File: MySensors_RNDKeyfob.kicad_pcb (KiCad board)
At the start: 2 copper layers, 27 x 42.9 mm, 21 parts, among them P1 CONN_01X01, P2 CONN_02X03, SW1 SW_SPST, SW2 SW_SPST, SW3 SW_SPST, SW4 SW_SPST, SW5 SW_SPST, U1 ATSHA204A, U2 RFM69HCW, U3 ATMEGA328P-MU

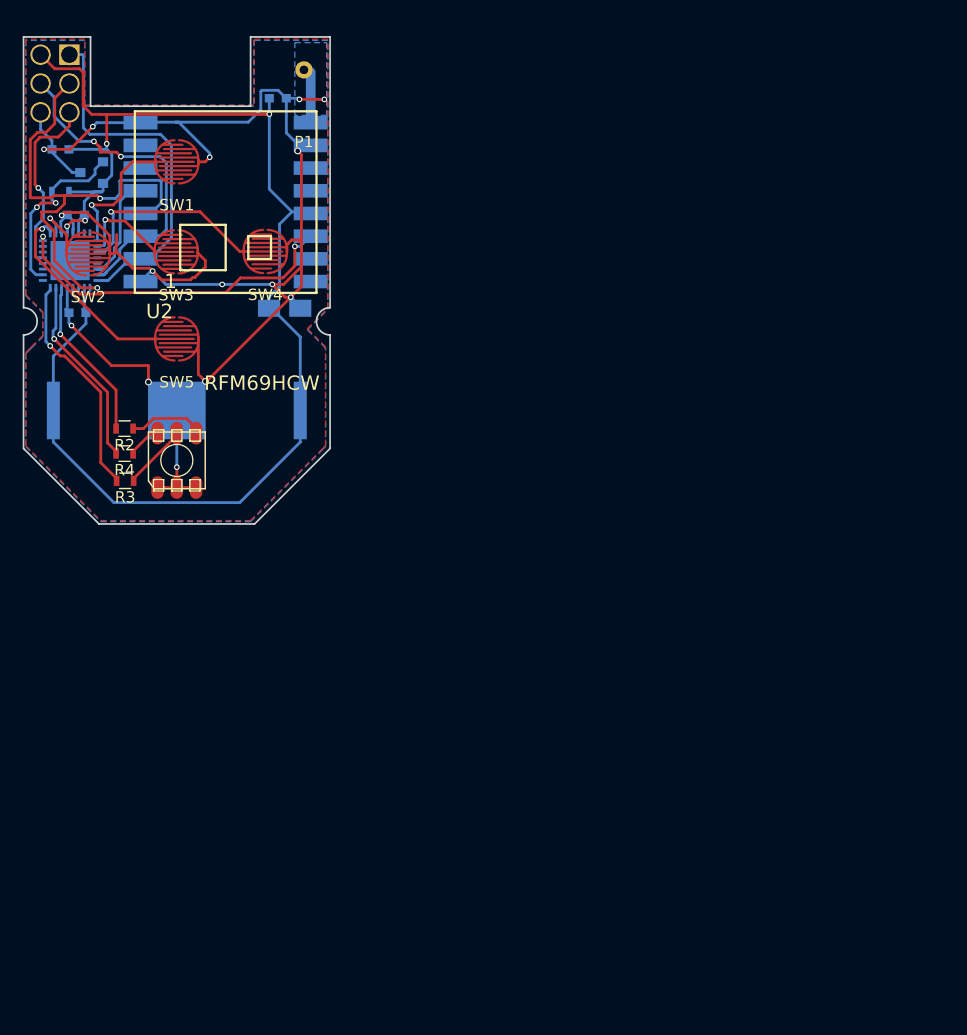
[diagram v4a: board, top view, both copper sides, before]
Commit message: Tiled with v-cut for production, added Gerbers
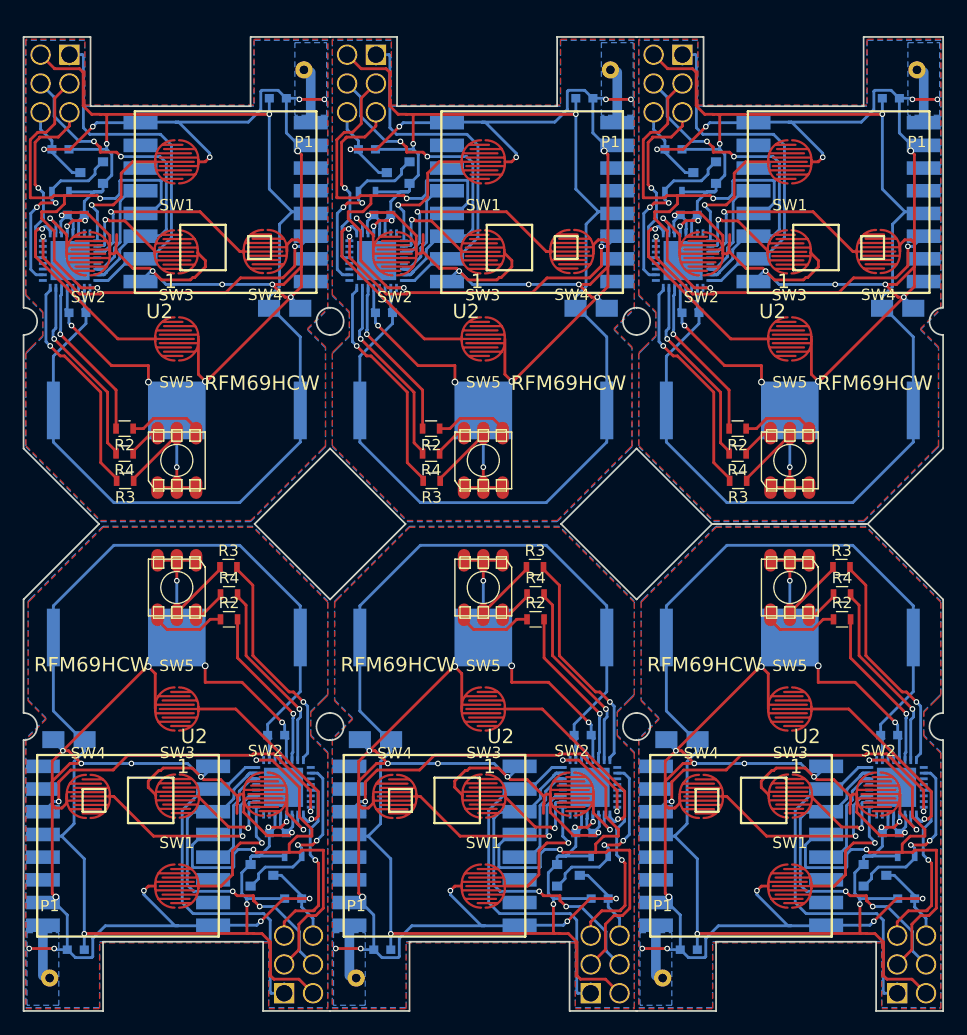
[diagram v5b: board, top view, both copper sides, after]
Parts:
- added BT1: Battery, parts:CR2032Holder, B.Cu at (254.0, 110.0)
- added BT1: Battery, parts:CR2032Holder, B.Cu at (227.0, 110.0)
- added BT1: Battery, parts:CR2032Holder, B.Cu at (200.0, 110.0)
- added BT1: Battery, parts:CR2032Holder, B.Cu at (254.0, 90.0)
- added BT1: Battery, parts:CR2032Holder, B.Cu at (227.0, 90.0)
- added C1: 100n, Capacitors_SMD:C_0603, B.Cu at (245.1, 137.5)
- added C1: 100n, Capacitors_SMD:C_0603, B.Cu at (218.1, 137.5)
- added C1: 100n, Capacitors_SMD:C_0603, B.Cu at (191.1, 137.5)
- added C1: 100n, Capacitors_SMD:C_0603, B.Cu at (262.9, 62.5)
- added C1: 100n, Capacitors_SMD:C_0603, B.Cu at (235.9, 62.5)
- added C2: 100n, Capacitors_SMD:C_0603, B.Cu at (264.2, 133.0)
- added C2: 100n, Capacitors_SMD:C_0603, B.Cu at (237.2, 133.0)
- added C2: 100n, Capacitors_SMD:C_0603, B.Cu at (210.2, 133.0)
- added C2: 100n, Capacitors_SMD:C_0603, B.Cu at (243.8, 67.0)
- added C2: 100n, Capacitors_SMD:C_0603, B.Cu at (216.8, 67.0)
- added C3: CP, Capacitors_Tantalum_SMD:CP_Tantalum_Case-A_EIA-3216-18_Reflow, B.Cu at (244.5, 119.0)
- added C3: CP, Capacitors_Tantalum_SMD:CP_Tantalum_Case-A_EIA-3216-18_Reflow, B.Cu at (217.5, 119.0)
- added C3: CP, Capacitors_Tantalum_SMD:CP_Tantalum_Case-A_EIA-3216-18_Reflow, B.Cu at (190.5, 119.0)
- added C3: CP, Capacitors_Tantalum_SMD:CP_Tantalum_Case-A_EIA-3216-18_Reflow, B.Cu at (263.5, 81.0)
- added C3: CP, Capacitors_Tantalum_SMD:CP_Tantalum_Case-A_EIA-3216-18_Reflow, B.Cu at (236.5, 81.0)
- added C4: 100n, Capacitors_SMD:C_0603, B.Cu at (262.9, 127.2)
- added C4: 100n, Capacitors_SMD:C_0603, B.Cu at (235.9, 127.2)
- added C4: 100n, Capacitors_SMD:C_0603, B.Cu at (208.9, 127.2)
- added C4: 100n, Capacitors_SMD:C_0603, B.Cu at (245.1, 72.8)
- added C4: 100n, Capacitors_SMD:C_0603, B.Cu at (218.1, 72.8)
- added C5: 100n, Capacitors_SMD:C_0603, B.Cu at (262.8, 118.6)
- added C5: 100n, Capacitors_SMD:C_0603, B.Cu at (235.8, 118.6)
- added C5: 100n, Capacitors_SMD:C_0603, B.Cu at (208.8, 118.6)
- added C5: 100n, Capacitors_SMD:C_0603, B.Cu at (245.2, 81.4)
- added C5: 100n, Capacitors_SMD:C_0603, B.Cu at (218.2, 81.4)
- added D1: LED_RGB, SparkFun-LED:LED-TRICOLOR-5050, F.Cu at (254.0, 105.6)
- added D1: LED_RGB, SparkFun-LED:LED-TRICOLOR-5050, F.Cu at (227.0, 105.6)
- added D1: LED_RGB, SparkFun-LED:LED-TRICOLOR-5050, F.Cu at (200.0, 105.6)
- added D1: LED_RGB, SparkFun-LED:LED-TRICOLOR-5050, F.Cu at (254.0, 94.4)
- added D1: LED_RGB, SparkFun-LED:LED-TRICOLOR-5050, F.Cu at (227.0, 94.4)
- added P1: CONN_01X01, parts:868MHz_Spring_Antenna, F.Cu at (242.8, 140.0)
- added P1: CONN_01X01, parts:868MHz_Spring_Antenna, F.Cu at (215.8, 140.0)
- added P1: CONN_01X01, parts:868MHz_Spring_Antenna, F.Cu at (188.8, 140.0)
- added P1: CONN_01X01, parts:868MHz_Spring_Antenna, F.Cu at (265.2, 60.0)
- added P1: CONN_01X01, parts:868MHz_Spring_Antenna, F.Cu at (238.2, 60.0)
- added P2: CONN_02X03, Pin_Headers:Pin_Header_Straight_2x03_Pitch2.54mm, B.Cu at (263.5, 141.3)
- added P2: CONN_02X03, Pin_Headers:Pin_Header_Straight_2x03_Pitch2.54mm, B.Cu at (236.5, 141.3)
- added P2: CONN_02X03, Pin_Headers:Pin_Header_Straight_2x03_Pitch2.54mm, B.Cu at (209.5, 141.3)
- added P2: CONN_02X03, Pin_Headers:Pin_Header_Straight_2x03_Pitch2.54mm, B.Cu at (244.5, 58.7)
- added P2: CONN_02X03, Pin_Headers:Pin_Header_Straight_2x03_Pitch2.54mm, B.Cu at (217.5, 58.7)
- added R1: 1K, Resistors_SMD:R_0603, B.Cu at (264.2, 129.2)
- added R1: 1K, Resistors_SMD:R_0603, B.Cu at (237.2, 129.2)
- added R1: 1K, Resistors_SMD:R_0603, B.Cu at (210.2, 129.2)
- added R1: 1K, Resistors_SMD:R_0603, B.Cu at (243.8, 70.8)
- added R1: 1K, Resistors_SMD:R_0603, B.Cu at (216.8, 70.8)
- added R2: R, Resistors_SMD:R_0603, F.Cu at (258.6, 108.4)
- added R2: R, Resistors_SMD:R_0603, F.Cu at (231.6, 108.4)
- added R2: R, Resistors_SMD:R_0603, F.Cu at (204.6, 108.4)
- added R2: R, Resistors_SMD:R_0603, F.Cu at (249.4, 91.6)
- added R2: R, Resistors_SMD:R_0603, F.Cu at (222.4, 91.6)
- added R3: R, Resistors_SMD:R_0603, F.Cu at (258.6, 103.8)
- added R3: R, Resistors_SMD:R_0603, F.Cu at (231.6, 103.8)
- added R3: R, Resistors_SMD:R_0603, F.Cu at (204.6, 103.8)
- added R3: R, Resistors_SMD:R_0603, F.Cu at (249.4, 96.2)
- added R3: R, Resistors_SMD:R_0603, F.Cu at (222.4, 96.2)
- added R4: R, Resistors_SMD:R_0603, F.Cu at (258.6, 106.2)
- added R4: R, Resistors_SMD:R_0603, F.Cu at (231.6, 106.2)
- added R4: R, Resistors_SMD:R_0603, F.Cu at (204.6, 106.2)
- added R4: R, Resistors_SMD:R_0603, F.Cu at (249.4, 93.8)
- added R4: R, Resistors_SMD:R_0603, F.Cu at (222.4, 93.8)
- added SW1: SW_SPST, parts:4mm_Rubber_Button, F.Cu at (254.0, 131.9)
- added SW1: SW_SPST, parts:4mm_Rubber_Button, F.Cu at (227.0, 131.9)
- added SW1: SW_SPST, parts:4mm_Rubber_Button, F.Cu at (200.0, 131.9)
- added SW1: SW_SPST, parts:4mm_Rubber_Button, F.Cu at (254.0, 68.1)
- added SW1: SW_SPST, parts:4mm_Rubber_Button, F.Cu at (227.0, 68.1)
- added SW2: SW_SPST, parts:4mm_Rubber_Button, F.Cu at (261.8, 123.8)
- added SW2: SW_SPST, parts:4mm_Rubber_Button, F.Cu at (234.8, 123.8)
- added SW2: SW_SPST, parts:4mm_Rubber_Button, F.Cu at (207.8, 123.8)
- added SW2: SW_SPST, parts:4mm_Rubber_Button, F.Cu at (246.2, 76.2)
- added SW2: SW_SPST, parts:4mm_Rubber_Button, F.Cu at (219.2, 76.2)
- added SW3: SW_SPST, parts:4mm_Rubber_Button, F.Cu at (254.1, 124.0)
- added SW3: SW_SPST, parts:4mm_Rubber_Button, F.Cu at (227.1, 124.0)
- added SW3: SW_SPST, parts:4mm_Rubber_Button, F.Cu at (200.1, 124.0)
- added SW3: SW_SPST, parts:4mm_Rubber_Button, F.Cu at (253.9, 76.0)
- added SW3: SW_SPST, parts:4mm_Rubber_Button, F.Cu at (226.9, 76.0)
- added SW4: SW_SPST, parts:4mm_Rubber_Button, F.Cu at (246.2, 124.0)
- added SW4: SW_SPST, parts:4mm_Rubber_Button, F.Cu at (219.2, 124.0)
- added SW4: SW_SPST, parts:4mm_Rubber_Button, F.Cu at (192.2, 124.0)
- added SW4: SW_SPST, parts:4mm_Rubber_Button, F.Cu at (261.8, 76.0)
- added SW4: SW_SPST, parts:4mm_Rubber_Button, F.Cu at (234.8, 76.0)
- added SW5: SW_SPST, parts:4mm_Rubber_Button, F.Cu at (254.0, 116.3)
- added SW5: SW_SPST, parts:4mm_Rubber_Button, F.Cu at (227.0, 116.3)
- added SW5: SW_SPST, parts:4mm_Rubber_Button, F.Cu at (200.0, 116.3)
- added SW5: SW_SPST, parts:4mm_Rubber_Button, F.Cu at (254.0, 83.7)
- added SW5: SW_SPST, parts:4mm_Rubber_Button, F.Cu at (227.0, 83.7)
- added U1: ATSHA204A, TO_SOT_Packages_SMD:SOT-23, B.Cu at (261.5, 130.9)
- added U1: ATSHA204A, TO_SOT_Packages_SMD:SOT-23, B.Cu at (234.5, 130.9)
- added U1: ATSHA204A, TO_SOT_Packages_SMD:SOT-23, B.Cu at (207.5, 130.9)
- added U1: ATSHA204A, TO_SOT_Packages_SMD:SOT-23, B.Cu at (246.5, 69.0)
- added U1: ATSHA204A, TO_SOT_Packages_SMD:SOT-23, B.Cu at (219.5, 69.0)
- added U2: RFM69HCW, SparkFun-RF:RFM69HCW-XXXS2, B.Cu at (249.7, 128.3)
- added U2: RFM69HCW, SparkFun-RF:RFM69HCW-XXXS2, B.Cu at (222.7, 128.3)
- added U2: RFM69HCW, SparkFun-RF:RFM69HCW-XXXS2, B.Cu at (195.7, 128.3)
- added U2: RFM69HCW, SparkFun-RF:RFM69HCW-XXXS2, B.Cu at (258.3, 71.7)
- added U2: RFM69HCW, SparkFun-RF:RFM69HCW-XXXS2, B.Cu at (231.3, 71.7)
- added U3: ATMEGA328P-MU, Housings_DFN_QFN:QFN-32-1EP_5x5mm_Pitch0.5mm, B.Cu at (263.4, 123.2)
- added U3: ATMEGA328P-MU, Housings_DFN_QFN:QFN-32-1EP_5x5mm_Pitch0.5mm, B.Cu at (236.4, 123.2)
- added U3: ATMEGA328P-MU, Housings_DFN_QFN:QFN-32-1EP_5x5mm_Pitch0.5mm, B.Cu at (209.4, 123.2)
- added U3: ATMEGA328P-MU, Housings_DFN_QFN:QFN-32-1EP_5x5mm_Pitch0.5mm, B.Cu at (244.6, 76.8)
- added U3: ATMEGA328P-MU, Housings_DFN_QFN:QFN-32-1EP_5x5mm_Pitch0.5mm, B.Cu at (217.6, 76.8)
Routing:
- net GND: track 157.4 -> 944.6 mm, vias 15 -> 90
- net /VCC: track 125.5 -> 753.2 mm, vias 4 -> 24
- net /SCK: track 43.6 -> 261.6 mm, vias 2 -> 12
- net /MISO: track 34.2 -> 205.1 mm
- net /D2: track 31.6 -> 189.3 mm, vias 2 -> 12
- net /MOSI: track 30.4 -> 182.3 mm, vias 2 -> 12
- net /A1: track 20.0 -> 119.7 mm, vias 1 -> 6
- net /D7: track 19.2 -> 115.0 mm, vias 1 -> 6
- net /D3: track 17.6 -> 105.7 mm, vias 1 -> 6
- net /A0: track 17.0 -> 102.0 mm, vias 1 -> 6
- net /RESET: track 16.0 -> 96.2 mm, vias 1 -> 6
- net /A3: track 15.9 -> 95.4 mm, vias 2 -> 12
- net /A7: track 14.5 -> 86.9 mm, vias 1 -> 6
- net /D10: track 12.7 -> 76.2 mm
- net /D5: track 11.8 -> 70.6 mm, vias 1 -> 6
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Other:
- board size 27 x 42.9 mm -> 81 x 85.8 mm
- board text added: "v-cut"
